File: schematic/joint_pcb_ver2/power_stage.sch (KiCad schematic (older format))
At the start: 39 parts, among them J3 Amp_Power, Q1 IRF530A, Q2 IRF530A, Q3 IRF530A, Q4 IRF530A, U1 HIP4082IP

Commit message: power 3.0 pcb layout
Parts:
- removed TP1, TP2, TP3, TP4: TestPoint, TestPoint:TestPoint_THTPad_D2.0mm_Drill1.0mm, symbol Connector:TestPoint
- added J3: Audio OUTPUT, TerminalBlock_Phoenix:TerminalBlock_Phoenix_PT-1,5-2-3.5-H_1x02_P3.50mm_Horizontal, symbol Connector:Screw_Terminal_01x02
- Q1, Q2, Q3, Q4: symbol dk_Transistors-FETs-MOSFETs-Single:IRF540NPBF -> joint_pcb-rescue:IRF540NPBF-dk_Transistors-FETs-MOSFETs-Single
- U3: renamed from U1; Digi-Key_PN 2156-HIP4082IP-IL-ND -> (none)
- renumbered C1 to C15, C2 to C16, C3 to C17, C4 to C18, C5 to C19, C8 to C20, C10 to C21, C11 to C22, J3 to J2, R10 to R21, R11 to R22, R1 to R23, R2 to R24, R3 to R25, R4 to R26, R5 to R27, R6 to R28, R7 to R29, R8 to R30, R9 to R31
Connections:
- wire segments 108 -> 107

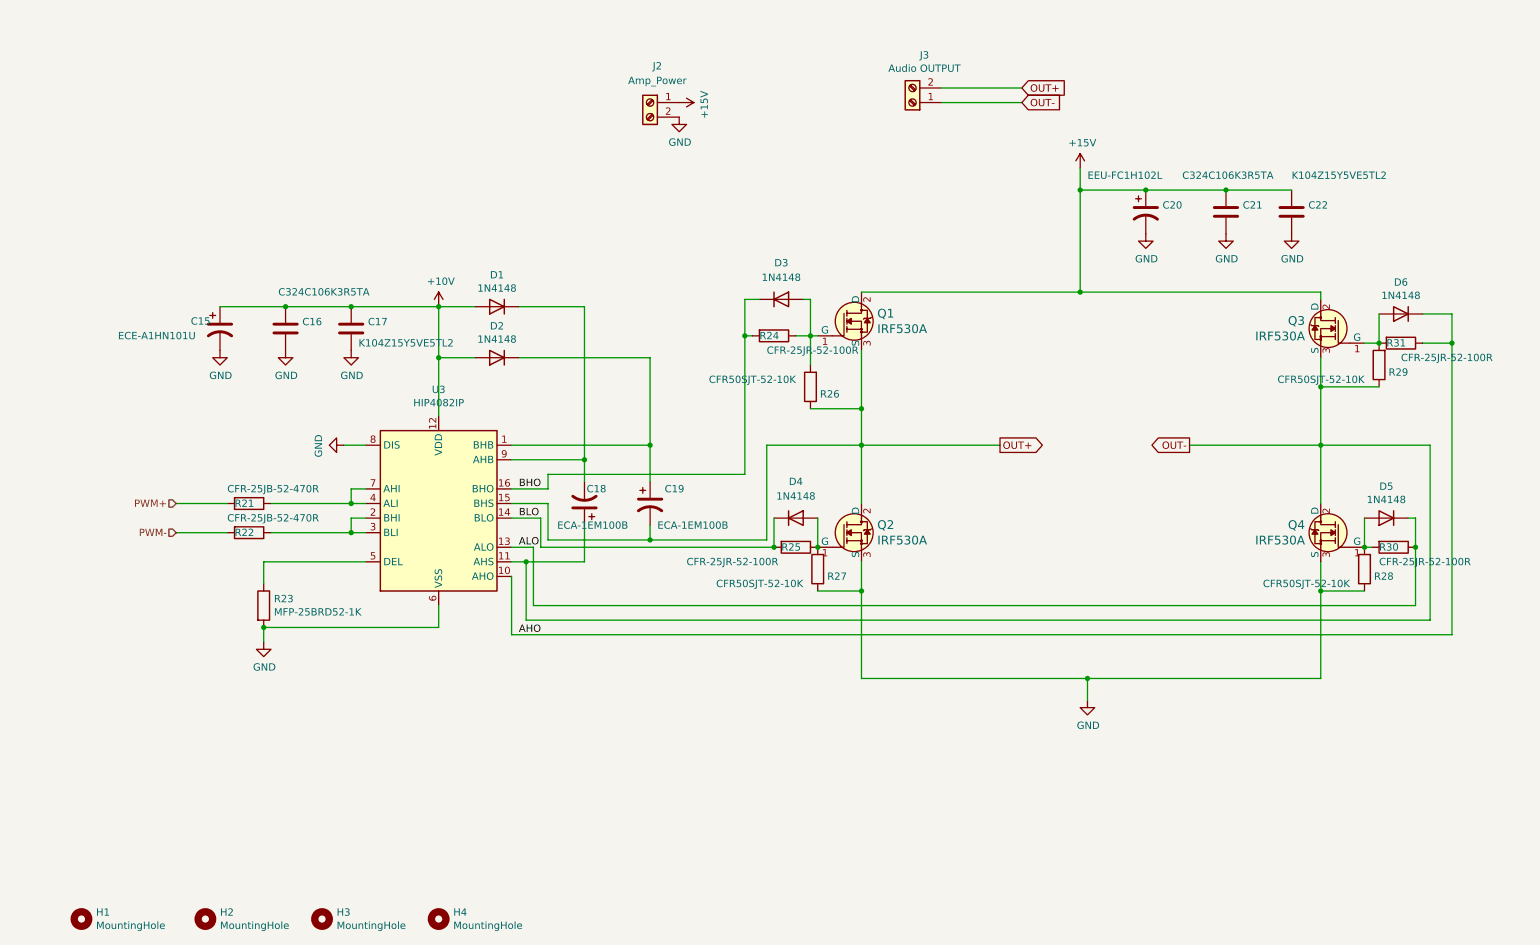
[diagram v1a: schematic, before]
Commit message: connect up 10V
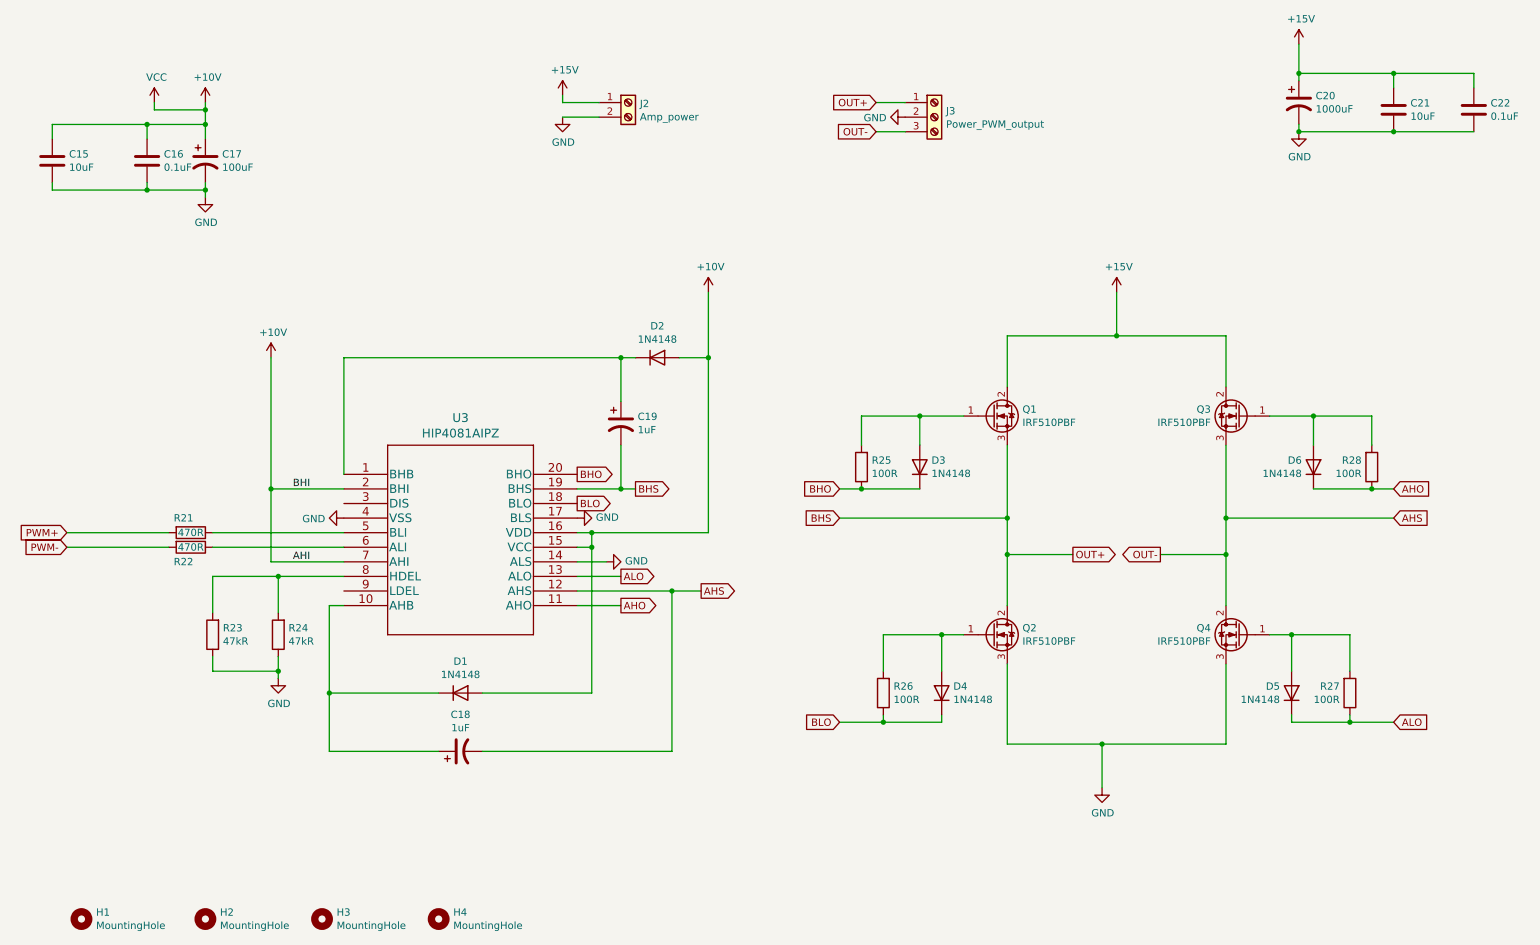
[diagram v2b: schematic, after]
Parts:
- removed C15: ECE-A1HN101U, Capacitor_THT:CP_Radial_D10.0mm_P5.00mm, symbol Device:CP1
- removed C17: K104Z15Y5VE5TL2, Capacitor_THT:C_Disc_D3.8mm_W2.6mm_P2.50mm, symbol Device:C
- removed D1, D2, D3, D4, D5, D6: 1N4148, Diode_THT:D_DO-35_SOD27_P7.62mm_Horizontal, symbol Diode:1N4148
- removed J3: Audio OUTPUT, TerminalBlock_Phoenix:TerminalBlock_Phoenix_PT-1,5-2-3.5-H_1x02_P3.50mm_Horizontal, symbol Connector:Screw_Terminal_01x02
- removed Q1, Q2, Q3, Q4: IRF530A, digikey-footprints:TO-220-3, symbol joint_pcb-rescue:IRF540NPBF-dk_Transistors-FETs-MOSFETs-Single
- removed R29: CFR50SJT-52-10K, Resistor_THT:R_Axial_DIN0207_L6.3mm_D2.5mm_P10.16mm_Horizontal, symbol Device:R
- removed R30, R31: CFR-25JR-52-100R, Resistor_THT:R_Axial_DIN0207_L6.3mm_D2.5mm_P10.16mm_Horizontal, symbol Device:R
- removed U3: HIP4082IP, Package_DIP:DIP-16_W7.62mm, symbol Driver_FET:HIP4082xP
- added C15: 10uF, Capacitor_THT:C_Disc_D3.8mm_W2.6mm_P2.50mm, symbol Device:C
- added C17: 100uF, Capacitor_THT:CP_Radial_D10.0mm_P5.00mm, symbol Device:CP1
- added D1, D2, D3, D4, D5, D6: 1N4148, Diode_THT:D_DO-35_SOD27_P7.62mm_Horizontal, symbol Device:D
- added J3: Power_PWM_output, TerminalBlock_Phoenix:TerminalBlock_Phoenix_PT-1,5-3-3.5-H_1x03_P3.50mm_Horizontal, symbol Connector:Screw_Terminal_01x03
- added Q1, Q2, Q3, Q4: IRF510PBF, Package_TO_SOT_THT:TO-220-3_Vertical, symbol Transistor_FET:IRF540N
- added U3: HIP4081AIPZ, footprints:HIP4081AIPZ, symbol HIP4081AIPZ:HIP4081AIPZ
- C16: value C324C106K3R5TA -> 0.1uF; Description 10uF 25V 10% -> 0.1uF 25V -20%,+80%; MPN (none) -> K104Z15Y5VE5TL2
- C18, C19: value ECA-1EM100B -> 1uF; footprint Capacitor_THT:CP_Radial_Tantal_D5.0mm_P5.00mm -> Capacitor_THT:CP_Radial_D4.0mm_P1.50mm; Description 10uF 25V 20% -> 1uF 50V 20%; MPN (none) -> ESS105M050AB2EA
- C20: value EEU-FC1H102L -> 1000uF; MPN (none) -> EEU-FC1H102L
- C21: value C324C106K3R5TA -> 10uF; MPN (none) -> C324C106K3R5TA
- C22: value K104Z15Y5VE5TL2 -> 0.1uF; MPN (none) -> K104Z15Y5VE5TL2
- J2: value Amp_Power -> Amp_power; Digi-Key_PN 277-1667-ND -> (none)
- R21, R22: value CFR-25JB-52-470R -> 470R; MPN (none) -> CFR-25JB-52-470R
- R23: value MFP-25BRD52-1K -> 47kR; Description 1k ohm 1% 1/4w -> (none)
- R24: value CFR-25JR-52-100R -> 47kR; Description 100 ohm 5% 1/4W -> (none)
- R25: value CFR-25JR-52-100R -> 100R; MPN (none) -> CFR-25JR-52-100R
- R26, R27, R28: value CFR50SJT-52-10K -> 100R; Description 10k ohm 5% 1/4W -> 100 ohm 5% 1/4W; MPN (none) -> CFR-25JR-52-100R
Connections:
- net +10V: now also C15.1, C17.1, D1.2 (A), D2.2 (A), U3.15 (VCC), U3.16 (VDD), U3.2 (BHI), U3.7 (AHI)
- net +15V: now also Q1.2 (D), Q3.2 (D)
- net AHO: now also R28.1, D6.1 (K), U3.11 (AHO)
- net ALO: now also R27.1, D5.1 (K), U3.13 (ALO)
- net BHO: now also R25.1, D3.1 (K), U3.20 (BHO); no longer R24.2
- net BLO: now also R26.1, D4.1 (K), U3.18 (BLO); no longer R25.2
- net GND: now also R23.1, R24.1, C15.2, C17.2, J3.2 (Pin_2), Q2.3 (S), Q4.3 (S), U3.14 (ALS), U3.17 (BLS), U3.4 (VSS); no longer R23.2, R27.1, R28.1
- net at C19.1: now also D2.1 (K), U3.1 (BHB)
- net at R22.1: now also U3.6 (ALI)
- net at R21.1: now also U3.5 (BLI)
- net AHS: now reaches C18.2
- net AHS: now also J3.3 (Pin_3), Q3.3 (S), Q4.2 (D), U3.12 (AHS)
- net at R26.2: now also D4.2 (A), Q2.1 (G); no longer R24.1
- net at R28.2: now also D6.2 (A), Q3.1 (G)
- net at R27.2: now also D5.2 (A), Q4.1 (G); no longer R25.1
- net OUT+ renamed BHS
- net BHS: now also J3.1 (Pin_1), Q1.3 (S), Q2.2 (D), U3.19 (BHS); no longer R26.1
- net OUT-: no longer names the net of C18.1
- net OUT-: now also D1.1 (K), U3.10 (AHB)
- new net: R23.2, R24.2, U3.8 (HDEL)
- new net: D3.2 (A), Q1.1 (G), R25.2
